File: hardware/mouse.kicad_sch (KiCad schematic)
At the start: 63 parts, among them J2 JSTPH, J3 USB_C_Receptacle_USB2.0_14P, SW1 SW_SPST, SW2 SW_SPST, SW3 SW_SPST, SW4 SW_SPST, SW5 SW_SPST, SW6 SW_SPST, SW7 RotaryEncoder, SW7 SW_SPST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

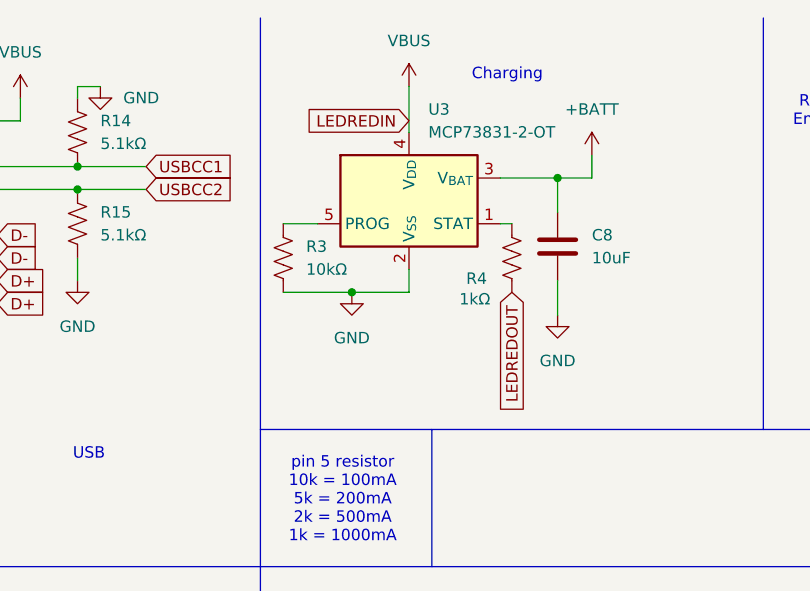
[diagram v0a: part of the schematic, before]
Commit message: forogt to fix charging
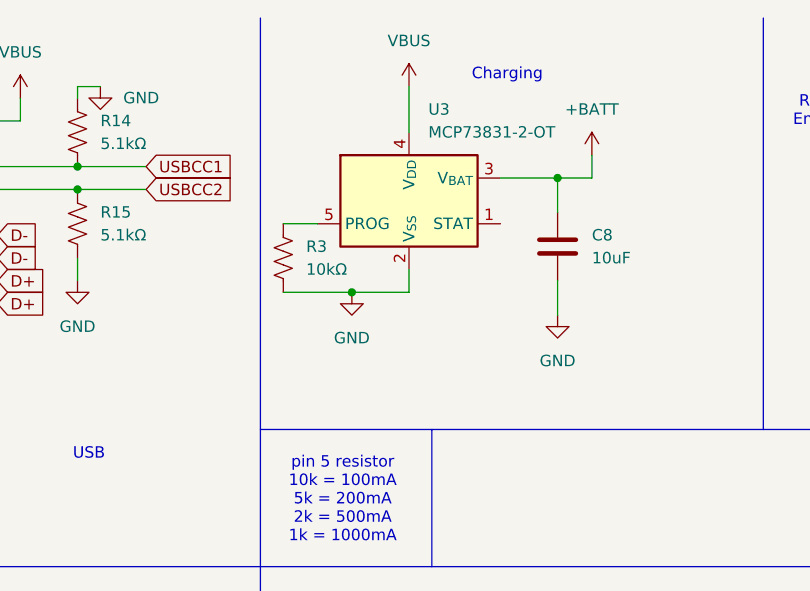
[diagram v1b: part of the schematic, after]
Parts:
- removed R4: 1kΩ, symbol Device:R_US
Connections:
- net VBUS: no longer D1.5 (AR)
- new net LEDREDIN: D1.5 (AR)
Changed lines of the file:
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@@
 	(wire
 		(pts
-			(xy 231.14 34.29) (xy 229.87 34.29)
-		)
-		(stroke
-			(width 0)
-			(type default)
-		)
-	)
-	(wire
-		(pts
 			(xy 217.17 116.84) (xy 222.25 116.84)
 		)
@@
 		)
 	)
-	(global_label "LEDREDIN"
-		(shape input)
-		(at 219.71 22.86 180)
-		(fields_autoplaced yes)
-		(effects
-			(font
-				(size 1.27 1.27)
-			)
-			(justify right)
-		)
-		(property "Intersheetrefs" "${INTERSHEET_REFS}"
-			(at 207.6534 22.86 0)
-			(effects
-				(font
-					(size 1.27 1.27)
-				)
-				(justify right)
-				(hide yes)
-			)
-		)
-	)
 	(global_label "LEDGREENIN"
 		(shape input)
@@
 		)
 	)
-	(global_label "LEDREDOUT"
-		(shape input)
-		(at 231.14 41.91 270)
-		(fields_autoplaced yes)
-		(effects
-			(font
-				(size 1.27 1.27)
-			)
-			(justify right)
-		)
-		(property "Intersheetrefs" "${INTERSHEET_REFS}"
-			(at 231.14 55.6599 90)
-			(effects
-				(font
-					(size 1.27 1.27)
-				)
-				(justify right)
-				(hide yes)
-			)
-		)
-	)
 	(global_label "Switch4"
 		(shape input)
@@
 					(unit 1)
 				)
-			)
-		)
-	)
-	(symbol
-		(lib_id "Device:R_US")
-		(at 231.14 38.1 180)
-		(unit 1)
-		(exclude_from_sim no)
-		(in_bom yes)
-		(on_board yes)
-		(dnp no)
-		(property "Reference" "R4"
-			(at 226.06 40.386 0)
-			(effects
-				(font
-					(size 1.27 1.27)
-				)
-				(justify right)
-			)
-		)
-		(property "Value" "1kΩ"
-			(at 225.298 42.672 0)
-			(effects
-				(font
-					(size 1.27 1.27)
-				)
-				(justify right)
-			)
-		)
-		(property "Footprint" ""
-			(at 230.124 37.846 90)
-			(effects
-				(font
-					(size 1.27 1.27)
-				)
-				(hide yes)
-			)
-		)
-		(property "Datasheet" "~"
-			(at 231.14 38.1 0)
-			(effects
-				(font
-					(size 1.27 1.27)
-				)
-				(hide yes)
-			)
-		)
-		(property "Description" "Resistor, US symbol"
-			(at 231.14 38.1 0)
-			(effects
-				(font
-					(size 1.27 1.27)
-				)
-				(hide yes)
-			)
-		)
-		(pin "1"
-		)
-		(pin "2"
-		)
-		(instances
-			(project "mouse"
-				(path "/533ef031-04e0-46be-a858-1bb00dbca72d"
-					(reference "R4")
-					(unit 1)
-				)

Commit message: fixed the led voltage and usb-c cc
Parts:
- removed D1: Inolux_IN-P55TATRGB, LED_SMD:LED_Inolux_IN-P55TATRGB_PLCC6_5.0x5.5mm_P1.8mm, symbol LED:Inolux_IN-P55TATRGB
- removed R14, R15: 5.1kΩ, symbol Device:R_US
- removed R16, R17: 220Ω, symbol Device:R_US
- added C40, C41: 10uF, symbol Device:C
- added C42: 1uF, symbol Device:C
- added D1: MBR1020VL, Diode_SMD:D_SOD-123F, symbol Diode:MBR1020VL
- added R4: 100kΩ, symbol Device:R_US
- added R6: 5.1kΩ, symbol Device:R_US
- added U6: SPX3819M5-L-5-0, Package_TO_SOT_SMD:SOT-23-5, symbol Regulator_Linear:SPX3819M5-L-5-0
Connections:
- net USBCC2 is gone; now on an unnamed net: J3.B5 (CC2)
- net +3.3V: no longer LED1.1 (VDD)
- net +BATT: now also D1.2 (A)
- net GND: now also C31.2, C40.2, C41.2, C42.2, R6.1, U6.2 (GND)
- net VBUS: now also C40.1, D1.1 (K), R4.1, U6.1 (IN)
- net USBCC1: no longer names the net of J3.A5 (CC1)
- net USBCC1: now also R6.2
- new net: R4.2, U6.3 (EN)
- new net +5V: C41.1, C42.1, LED1.1 (VDD), U6.5 (OUT)
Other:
- note removed: "LED"
- moved on the sheet: C12, C19, C20, C21, C22, C23, C26, C27, J2, LED1, R10, R11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

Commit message: all pcb routing done (i got carried away)
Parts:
- removed C40, C9: 10uF, symbol Device:C
- removed D1, D2: MBR1020VL, Diode_SMD:D_SOD-123F, symbol Diode:MBR1020VL
- added C43: 10uF, Capacitor_SMD:C_0805_2012Metric_Pad1.18x1.45mm_HandSolder, symbol Device:C
- added D5: MBR1020VL, Diode_SMD:D_SOD-123F, symbol Diode:MBR1020VL
- added SW9: SW_SPST, Button_Switch_SMD:SW_SPST_CK_RS282G05A3, symbol Switch:SW_SPST
- A1: footprint (none) -> custom:PAW3395
- C1, C10, C11, C12, C15, C16, C17, C18, C2, C24, C25, C26, C27, C3, C31, C4, C41, C42, C5, C6, C7, C8: footprint (none) -> Capacitor_SMD:C_0805_2012Metric_Pad1.18x1.45mm_HandSolder
- C19, C20, C21, C22, C23: value 1uF -> 100nF; footprint (none) -> Capacitor_SMD:C_0805_2012Metric_Pad1.18x1.45mm_HandSolder
- J2: footprint (none) -> custom:JSTPH2PINSMTRIGHTANGLECONNECTOR
- J3: footprint (none) -> Connector_USB:USB_C_Receptacle_Amphenol_12401548E4-2A
- LED1: footprint SK6812MINIE -> custom:SK6812MINIE
- R1, R2, R20, R21, R4, R5, R6, R8: footprint (none) -> Resistor_SMD:R_0805_2012Metric_Pad1.20x1.40mm_HandSolder
- R10, R11, R12, R13, R9: value 1.5kΩ -> 10kΩ; footprint (none) -> Resistor_SMD:R_0805_2012Metric_Pad1.20x1.40mm_HandSolder
- R3: value 10kΩ -> 2kΩ; footprint (none) -> Resistor_SMD:R_0805_2012Metric_Pad1.20x1.40mm_HandSolder
- SW1, SW2, SW4, SW5: footprint (none) -> custom:SW_Tactile_SPDT_Omron_D2F
- SW3: footprint (none) -> Button_Switch_THT:SW_PUSH_6mm
- SW6, SW7: footprint (none) -> Capacitor_SMD:C_0402_1005Metric
- SW8: renamed from SW7; footprint (none) -> custom:EC10E1220503
- Y1: footprint (none) -> custom:FC135327680KAA
- Y2: footprint (none) -> custom:ABM8A32000MHZD2YT3
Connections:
- net +3.3V: now also A1.7 (VDDIO); no longer A1. (MOTION)
- net +5V: now also C43.1
- net GND: now also A1.3 (GND), A1.8 (GNDIO), C43.2; no longer A1. (MOTION)
- net MISO: now also A1.12 (MISO); no longer A1. (MOTION)
- net MOSI: now also A1.11 (MOSI); no longer A1. (MOTION)
- net MOTION: now also A1.9 (MOTION); no longer A1. (MOTION)
- net MSNCS: now also A1.13 (NCS); no longer A1. (MOTION)
- net NRESET: now also A1.14 (NRESET); no longer A1. (MOTION)
- net SCLK: now also A1.10 (SCLK); no longer A1. (MOTION)
- net VBUS: now also D5.2 (A); no longer C15.1, D3.1 (K), R4.1, R5.1, R8.1, U2.1 (IN), U4.1 (IN), U6.1 (IN)
- net VDD_1.9V: now also A1.4 (VDD); no longer A1. (MOTION)
- net at R2.2: now also A1.15 (LED_P); no longer A1. (MOTION)
- net at C1.1, C2.1: now also A1.5 (VDDREG); no longer A1. (MOTION)
- new net: C15.1, R4.1, R5.1, R8.1, SW9.2 (B), U2.1 (IN), U4.1 (IN), U6.1 (IN)
- new net: D3.1 (K), D5.1 (K), SW9.1 (A)
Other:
- moved on the sheet: C15, D3, J2, R8
